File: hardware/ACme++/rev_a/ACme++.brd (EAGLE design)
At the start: 72.6 x 47.1 mm, 52 parts, among them J3 MA02-1, SW1 SWITCH_SPDP, T1 NCHAN_MOSFET, T2 NCHAN_MOSFET, T3 NCHAN_MOSFET, U1 ADE7753, U2 LTC3588_, U3 FM25LB, X1 ECS-35-17-5PX-TR

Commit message: working on relay
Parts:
- removed C13: 0.1uF, rcl:C0603
- removed R24, R25, R26: 4.7k, rcl:R0603
- removed TP11, TP12, TP7: WHITE, con-lstb:MA01-1
- removed TP13: GREEN, con-lstb:MA01-1
- removed U3: FM25LB, coilcube:SOIC_8
- added D1: DIODE_MMBD914, powercube:SOT-23
- added K1: S216S01F, powercube:RELAY_SX16S0X
- added R10: 100k, SparkFun:0603-RES
- added R9: (no value), SparkFun-Resistors:0805
- added U$1: FDV301N, powercube:SOT-23
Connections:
- removed net FRAM_CS: R24.1, TP13.1, U3.P1
- removed net FRAM_HOLD: R25.1, U3.P7
- removed net FRAM_WP: R26.1, U3.P3
- removed net MISO0: TP11.1, U3.P2
- removed net MOSI0: TP7.1, U3.P5
- removed net SCK0: TP12.1, U3.P6
- new net N$13: D1.3, K1.3, R9.1
- new net N$4: D1.1, K1.4, U$1.3
- new net RELAY_CTRL: R10.2, U$1.1
- net +3V3: no longer C13.1, R24.2, R25.2, R26.2, U3.P8
- net 3V3: now also R10.1
- net 5V: now also R9.2
- net GND: now also U$1.2; no longer C13.2, U3.P4
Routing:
- net FRAM_CS: track 44.4 -> 0.00 mm, vias 2 -> 0
- net FRAM_HOLD: track 33.7 -> 0.00 mm, vias 2 -> 0
- net MISO0: track 23.1 -> 0.00 mm, vias 2 -> 0
- net SCK0: track 22.2 -> 0.00 mm
- net MOSI0: track 20.7 -> 0.00 mm, vias 3 -> 0
- net FRAM_WP: track 17.8 -> 0.00 mm
- net +3V3: track 131.1 -> 122.1 mm

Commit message: working on ac connections
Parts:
- added C13, C22, C23: 33nF, SparkFun-Passives:0805
- added J1: AC-PLUG, powercube:AC_MALE_PINS
- added J2, J4, J5: WIRE_HOLE-14AWG, powercube:WIRE_HOLE-14AWG
- added L2, L3: EMI_SUPRESSION_FERRITE_BEAD, powercube:L1806
- added L4: 35F0121-0SR-10, powercube:35F0102
- added R11: .001, SparkFun-Resistors:R2512
- added R12, R13: 1k, SparkFun-Resistors:0805
- added R14: 499k, SparkFun-Resistors:0805
- added R15: 1k, SparkFun-Resistors:0603-RES
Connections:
- new net EARTH_GND: J1.GND, J1.GND_TAB, J5.P$1
- new net LOAD_NEUTRAL: J4.P$1, L3.P$1, R11.2
- new net LOAD_PHASE: J2.P$1, K1.2
- new net N$14: L2.P$2, R12.1
- new net N$16: L3.P$2, R13.1
- new net N$17: L4.2, R14.1
- new net WALL_NEUTRAL: J1.N1, J1.N10, J1.N11, J1.N2, J1.N3, J1.N4, J1.N5, J1.N6, J1.N7, J1.N8, J1.N9, J1.NEUTRAL, L2.P$1, R11.1
- new net WALL_PHASE: J1.N12, J1.P1, J1.P10, J1.P11, J1.P12, J1.P2, J1.P3, J1.P4, J1.P5, J1.P6, J1.P7, J1.P8, J1.P9, J1.PHASE, K1.1, L4.1
- net GND: now also C13.2, C22.2, C23.2, R15.1
- net V1N: now also C13.1, R12.2
- net V1P: now also C22.1, R13.2
- net V2P: now also C23.1, R14.2, R15.2

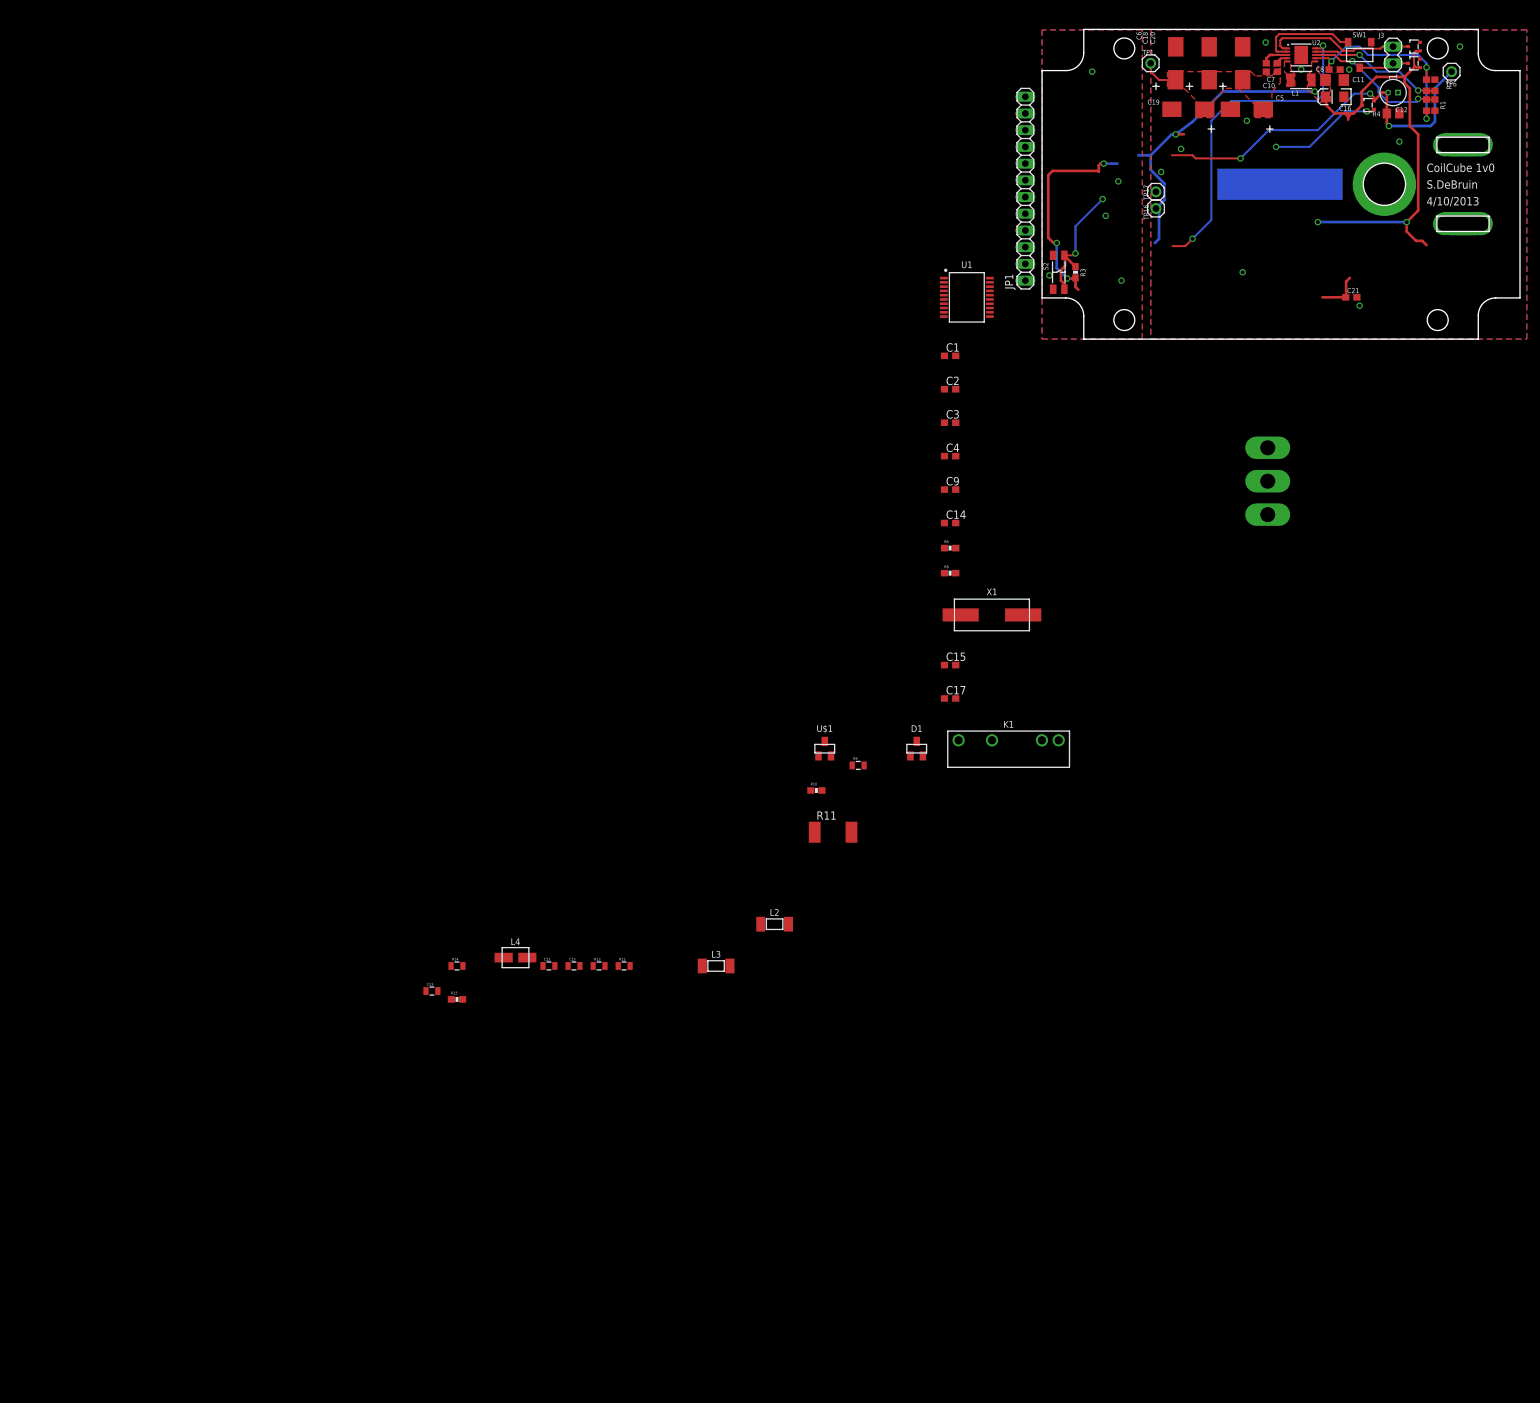
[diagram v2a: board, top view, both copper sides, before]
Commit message: power supplies fleshed out
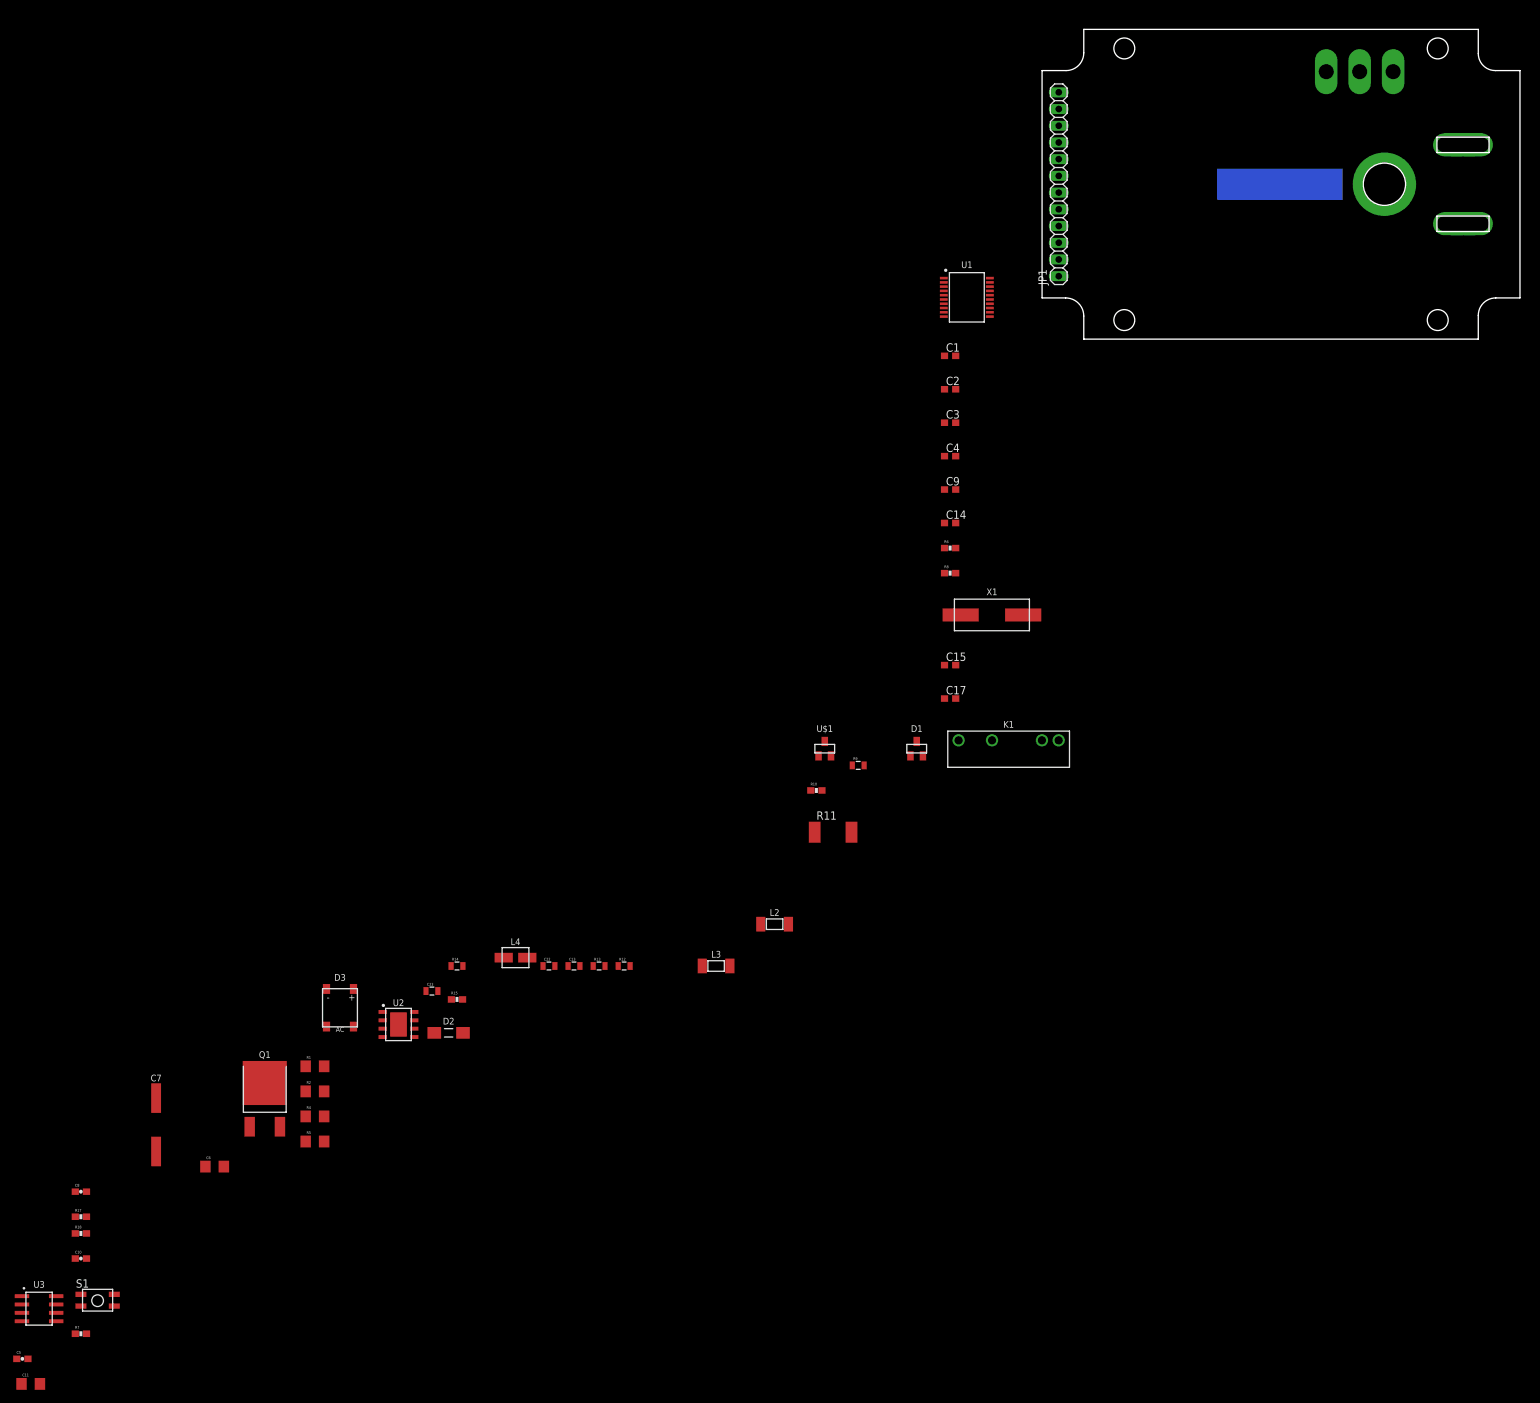
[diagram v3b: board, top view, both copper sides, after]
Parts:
- removed C12: 2.2uF, coilcube:CPOL_EEA_1MM5
- removed C16: 47uF, SparkFun-Passives:EIA3216
- removed C18, C19, C20: 100uF 25V, coilcube:2917_CAP_POL
- removed C21: 0.1uF, rcl:C0603
- removed J3: MA02-1, con-lstb:MA02-1
- removed L1: 10uH, SparkFun-Passives:1210
- removed R3: 10k, SparkFun:0603-RES
- removed S2: SWITCH-OFF-MOM, p498:SWITCH-OFF-MOM
- removed SW1: SWITCH_SPDP, coilcube:SWITCH_SPDP
- removed T1, T2, T3: NCHAN_MOSFET, Power_Metering:NCHAN_MOSFET
- removed TP1: ORANGE, con-lstb:MA01-1
- removed TP16: RED, con-lstb:MA01-1
- removed TP17: BLACK, con-lstb:MA01-1
- removed TP6: BLUE, con-lstb:MA01-1
- added D2: SMAJ_TVS, powercube:DO214_TVS
- added D3: CD2320-BB11000, powercube:CD2320
- added Q1: STGD5NB120SZT4, powercube:DPAK
- added R17: 113k, SparkFun-Resistors:0603-RES
- added R18: 12.4k, SparkFun-Resistors:0603-RES
- added S1: EVQP2, epic:EVQP2
- added U3: TDA3664AT, powercube:SOIC_8
- C10: device rcl:C0603 -> SparkFun-Passives:0603-CAP
- C11: value 10uF -> 47uF; device rcl:C1206 -> SparkFun-Passives:1206
- C5: value 100uF 25V -> 1uF; device coilcube:2917_CAP_POL -> SparkFun-Passives:0603-CAP
- C6: value 100uF 25V -> 1uF; device coilcube:2917_CAP_POL -> SparkFun-Passives:1206
- C7: value 1uF -> 470uF; device rcl:C0603 -> powercube:CAP_SM_10MM
- C8: value 4.7uF -> 0.1uF; device rcl:C0603 -> SparkFun-Passives:0603-CAP
- R1: value 0 -> 200k; device rcl:R0603 -> SparkFun-Resistors:1206
- R2: value NP -> 200k; device rcl:R0603 -> SparkFun-Resistors:1206
- R4: value 4.7M -> 510k; device rcl:R0805 -> SparkFun-Resistors:1206
- R5: value NP -> 510k; device rcl:R0603 -> SparkFun-Resistors:1206
- R7: value 0 -> 10k; device rcl:R0603 -> SparkFun:0603-RES
- U2: value LTC3588_ -> SR086SG-G; device SparkFun-PowerIC:MSOP-10-GNDPAD -> powercube:SR086
- moved C11 280.2 mm to (-153.7, -158.8)
- moved R7 279.9 mm to (-146.1, -151.1), turned to 0 degrees
- moved C5 265.8 mm to (-154.9, -154.9), turned to 0 degrees
- moved C8 255.7 mm to (-146.1, -129.5)
- moved C10 255.5 mm to (-146.1, -139.7), turned to 0 degrees
- moved C7 234.0 mm to (-134.6, -119.4), turned to 0 degrees
- moved R5 233.0 mm to (-110.5, -121.9), turned to 0 degrees
- moved R2 226.8 mm to (-110.5, -114.3), turned to 0 degrees
- moved R4 223.8 mm to (-110.5, -118.1), turned to 0 degrees
- moved R1 223.3 mm to (-110.5, -110.5), turned to 0 degrees
- moved C6 222.3 mm to (-125.7, -125.7), turned to 0 degrees
- moved U2 201.3 mm to (-97.8, -104.1), turned to 0 degrees
- moved J5 70.0 mm to (53.3, 40.6), turned to 90 degrees
- moved J4 63.8 mm to (48.3, 40.6), turned to 90 degrees
- moved J2 57.8 mm to (43.2, 40.6), turned to 90 degrees
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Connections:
- removed net +3V3: C11.1, C16.A, C21.1, L1.2, T1.G, T2.D, T3.G, TP16.1, U2.6
- removed net D0: R5.1, R7.1, U2.9
- removed net D1: R1.1, R2.1, U2.8
- removed net FTDIVDD: R3.2
- removed net N$2: S2.P$1, S2.P$3
- removed net N$20: L1.1, U2.5
- removed net PGOOD: U2.10
- removed net PZ1: J3.2, T1.D, U2.1
- removed net PZ2: SW1.P1, U2.2
- removed net RST: R3.1, S2.P$2, S2.P$4
- removed net TIME_CTL: T2.G
- removed net VCAP: C10.1, C18.+, C19.+, C20.+, C5.+, C6.+, C7.1, TP1.1, U2.4
- removed net VIN2: C8.1, R1.2, R5.2, U2.7
- removed net VTIMER: C12.+, R4.2, T2.S, TP6.1
- new net 5V0: C11.1, U3.1
- new net N$18: R1.1, R2.2
- new net N$19: R5.1, U2.1
- new net N$21: R4.1, R5.2
- new net N$24: C10.2, U2.7
- new net N$26: R17.1, R18.2, U2.5
- new net USER_RELAY_CTRL: R7.2, S1.P$2, S1.P$4
- new net VDC: C10.1, C5.1, C6.1, C7.+, Q1.P$3, R17.2, U2.6, U3.8
- net 3V3: now also C8.1, S1.P$1, S1.P$3, U2.4
- net GND: now also C5.2, C6.2, C7.-, D3.4, R18.1, R2.1, R7.1, U2.2, U2.3, U2.PAD, U3.3; no longer C10.2, C12.-, C16.C, C18.-, C19.-, C20.-, C21.2, C5.-, C6.-, R2.2, R4.1, R7.2, SW1.P3, T1.S, T3.S, TP17.1, U2.GND
- net N$1: now also D3.3, Q1.P$2, R1.2, R4.2; no longer J3.1, SW1.P2, T3.D
- net N$22: now also Q1.P$1, U2.8; no longer C7.2, U2.3
- net WALL_NEUTRAL: now also D2.CATHODE, D3.2
- net WALL_PHASE: now also D2.ANODE, D3.1
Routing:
- net +3V3: track 122.1 -> 0.00 mm, vias 4 -> 0
- net VTIMER: track 59.6 -> 0.00 mm, vias 3 -> 0
- net PGOOD: track 50.3 -> 0.00 mm, vias 2 -> 0
- net FTDIVDD: track 32.3 -> 0.00 mm, vias 3 -> 0
- net VIN2: track 32.0 -> 0.00 mm, vias 3 -> 0
- net PZ1: track 22.7 -> 0.00 mm
- net D1: track 22.0 -> 0.00 mm, vias 2 -> 0
- net D0: track 20.7 -> 0.00 mm, vias 2 -> 0
- net RST: track 20.0 -> 0.00 mm, vias 2 -> 0
- net TIME_CTL: track 17.2 -> 0.00 mm, vias 2 -> 0
- net PZ2: track 15.5 -> 0.00 mm
- net N$1: track 7.64 -> 0.00 mm
- net VCAP: track 7.55 -> 0.00 mm
- net N$22: track 4.14 -> 0.00 mm
- removed copper zone on layer 1, net +3V3
- removed copper zone on layer 1, net GND
- removed copper zone on layer 16, net GND
- removed copper zone on layer 1, net IGND
- removed copper zone on layer 16, net IGND
- removed copper zone on layer 1, net N$20
- removed copper zone on layer 1, net VCAP
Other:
- board text removed: "4/10/2013"
- board text removed: "CoilCube 1v0"
- board text removed: "S.DeBruin"

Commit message: progress
cleaned up schematic a bit

initial arragnment on pcb
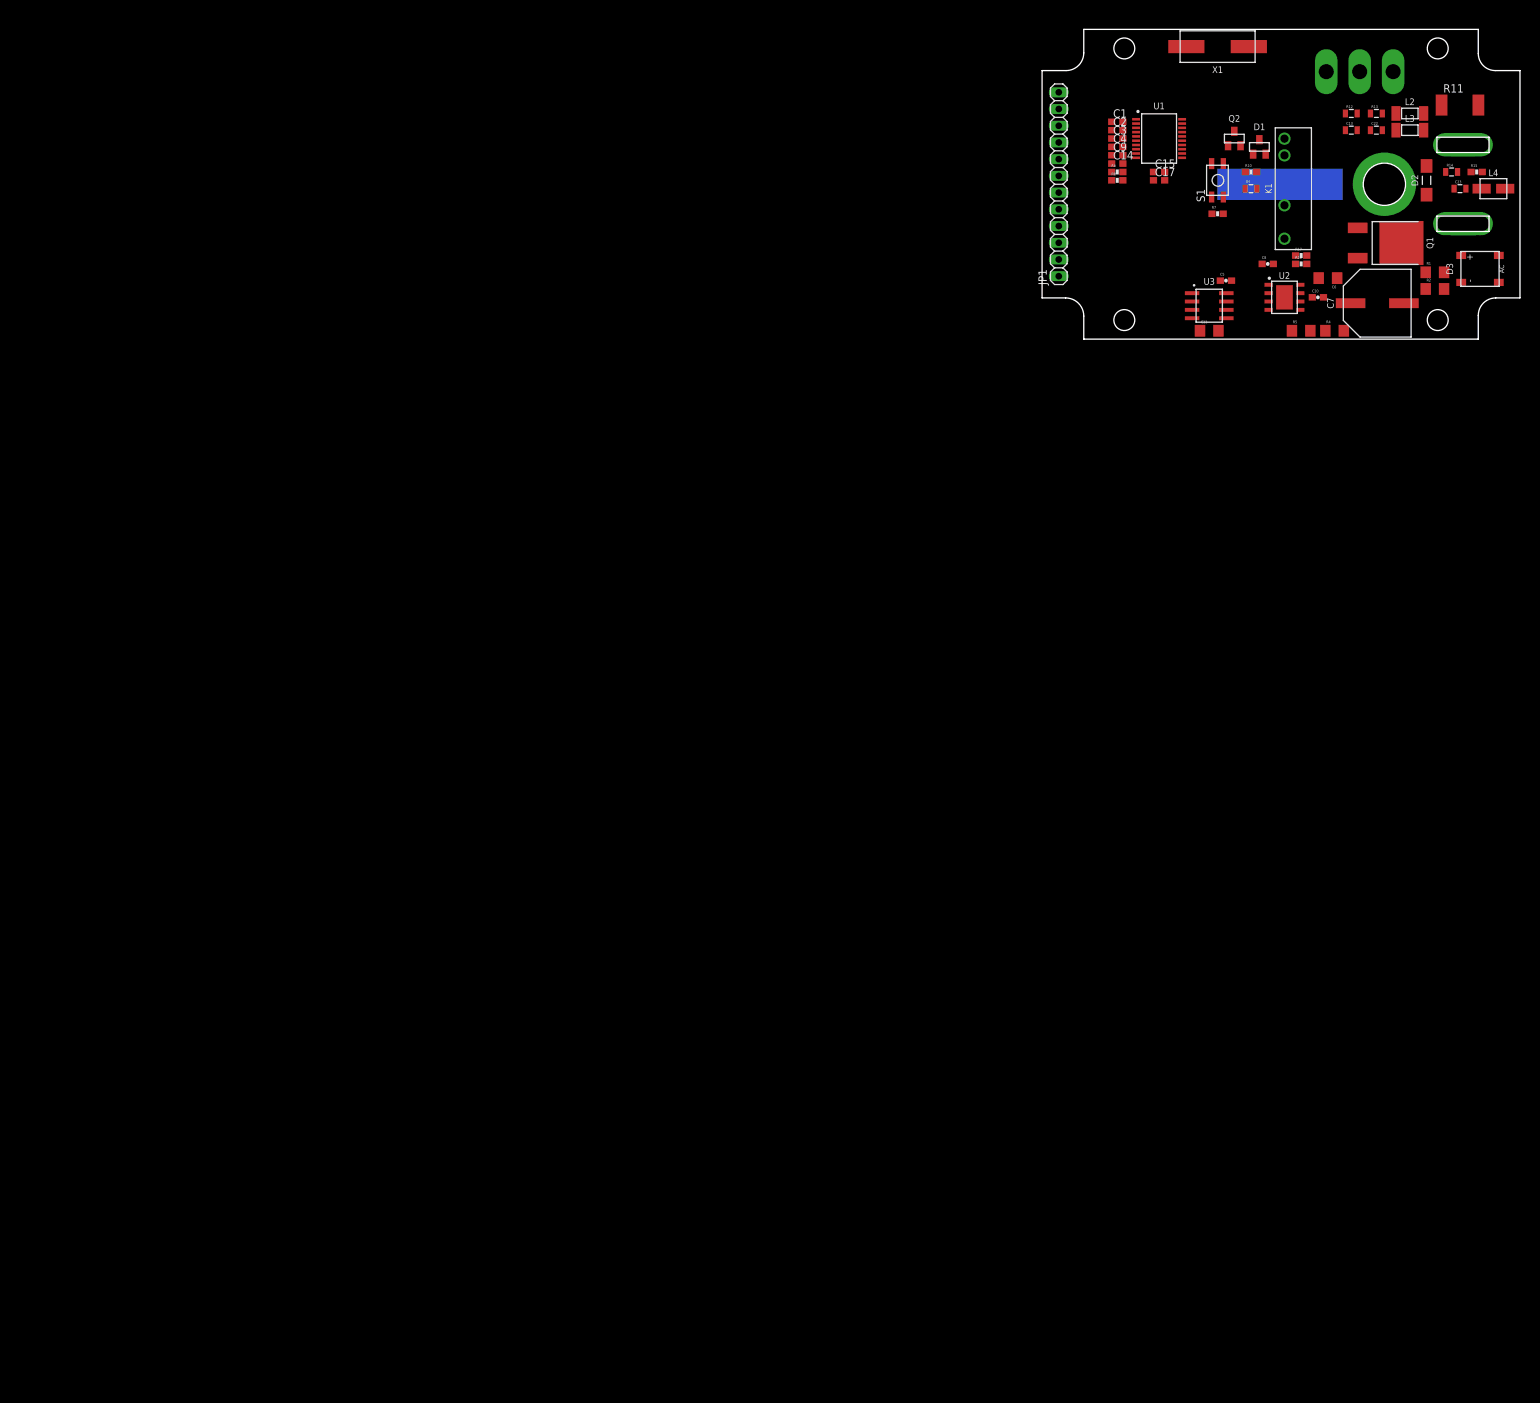
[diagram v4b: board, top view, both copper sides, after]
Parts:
- removed U$1: FDV301N, powercube:SOT-23
- added Q2: FDV301N, powercube:SOT-23
- moved C5 245.5 mm to (27.9, 8.89)
- moved R7 242.5 mm to (26.7, 19.1)
- moved S1 240.7 mm to (26.7, 24.1), turned to 90 degrees
- moved C11 240.2 mm to (25.4, 1.27)
- moved C10 238.0 mm to (41.9, 6.35)
- moved R18 236.8 mm to (39.4, 11.4)
- moved R17 236.0 mm to (39.4, 12.7)
- moved U3 234.2 mm to (25.4, 5.08)
- moved C8 228.9 mm to (34.3, 11.4)
- moved C7 223.6 mm to (50.9, 5.46), turned to 90 degrees
- moved C6 216.4 mm to (43.4, 9.27), turned to 180 degrees
- moved Q1 214.8 mm to (54.6, 14.6), turned to 270 degrees
- moved R2 209.3 mm to (59.7, 7.62)
- moved R1 208.6 mm to (59.7, 10.2)
- moved D3 206.4 mm to (66.5, 10.7), turned to 90 degrees
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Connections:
- removed net 5V: C1.1, C2.1, R6.2, R8.1, R9.2, U1.P$2
- removed net N$10: JP1.8
- removed net N$6: JP1.4
- removed net N$7: JP1.5
- removed net N$8: JP1.6
- removed net N$9: JP1.7
- removed net V2N: U1.P$6
- net !ADE_CS: now also JP1.4, U1.17; no longer U1.P$17
- net !ADE_IRQ: now also JP1.5, U1.14; no longer U1.P$14
- net !RESET: now also U1.1; no longer U1.P$1
- net 5V0: now also C1.1, C2.1, R6.2, R8.1, R9.2, U1.2
- net ADE_CF: now also JP1.7, U1.11; no longer U1.P$11
- net ADE_ZX: now also JP1.6, U1.12; no longer U1.P$12
- net GND: now also Q2.2, U1.10, U1.8; no longer U$1.2, U1.P$10, U1.P$8
- net MISO: now also U1.19; no longer U1.P$19
- net MOSI: now also U1.20; no longer U1.P$20
- net N$11: now also U1.9; no longer U1.P$9
- net N$15: now also U1.16; no longer U1.P$16
- net N$3: now also U1.15; no longer U1.P$15
- net N$4: now also Q2.3; no longer U$1.3
- net N$5: now also U1.3; no longer U1.P$3
- net RELAY_CTRL: now also Q2.1; no longer U$1.1
- net SCLK: now also U1.18; no longer U1.P$18
- net USER_RELAY_CTRL: now also JP1.8
- net V1N: now also U1.5, U1.6; no longer U1.P$5
- net V1P: now also U1.4; no longer U1.P$4
- net V2P: now also U1.7; no longer U1.P$7
